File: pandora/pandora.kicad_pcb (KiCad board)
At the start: 2 copper layers, 121.9 x 106.7 mm, 176 parts, among them J1 SMA, J2 PinHeader_100mil_01x04, J3 JST-SH_2, J4 TX3 / MTA-156-3, J5 Conn_ARM_JTAG_SWD_10, J6 USB_B_Mini, Q1 DMP1045U, SW1 GF-126-0317, SW10 PTS645-S-H-50-SMTR92-LFS, SW11 PTS645-S-H-50-SMTR92-LFS, SW12 PTS645-S-H-50-SMTR92-LFS, SW13 PTS645-S-M-43-SMTR92-LFS, SW14 PTS645-S-K-50-SMTR92-LFS, SW15 PTS645-S-K-50-SMTR92-LFS, SW16 PTS645-S-K-50-SMTR92-LFS, SW17 PTS645-S-K-50-SMTR92-LFS, SW18 PTS526-S-K-15-SMTR92-LFS, SW2 PTS645-S-H-50-SMTR92-LFS, SW3 PTS645-S-H-50-SMTR92-LFS, SW4 PTS645-S-H-50-SMTR92-LFS, SW5 PTS645-S-H-50-SMTR92-LFS, SW6 PTS645-S-H-50-SMTR92-LFS, SW7 PTS645-S-H-50-SMTR92-LFS, SW8 PTS645-S-H-50-SMTR92-LFS, SW9 PTS645-S-M-43-SMTR92-LFS, U1 LM1086CS-ADJ, U10 ADM811ZARTZ, U11 LCD_Adafruit_16x02_Neg_RGB, U12 MCP73831-2-OT, U13 MCP1642D-50, U2 MCP1702T-3302, U3 MCP1702T-3302, U4 MCP6001, U5 MPU-9250, U6 ULN2003D, U7 74LCX245, U8 CC2652R, U9 74LVC1G08, Y1 NC26_32.768k, Y2 FA-238_48M

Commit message: Continue layout
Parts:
- moved R19 10.3 mm to (-49.9, 100.1), turned to 90 degrees
- moved RV1 3.41 mm to (-104.0, 83.3)
- moved NT3 2.41 mm to (-13.3, 107.3)
- moved C33 2.16 mm to (-30.6, 90.9), turned to 270 degrees
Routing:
- net /keypad/KPD_IN2: track 16.5 -> 56.2 mm
- net /connectors/LCD_OUT_CNTR: track 0.00 -> 36.9 mm
- net Net-(D2-Pad2): track 0.00 -> 35.5 mm
- net +5V: track 13.0 -> 47.4 mm
- net Net-(D4-Pad2): track 0.00 -> 28.2 mm
- net VMCU: track 48.9 -> 76.4 mm, vias 3 -> 7
- net VIN: track 4.79 -> 23.6 mm
- net /connectors/SERVO_PWM: track 32.0 -> 44.7 mm, vias 0 -> 2
- net /connectors/JTAG_~RESET: track 5.91 -> 17.3 mm
- net VSERVO: track 9.82 -> 19.1 mm
- net GNDBAT: track 18.5 -> 27.1 mm
- net GNDIN: track 16.6 -> 25.0 mm
- net /keypad/KPD_IN4: track 28.9 -> 35.8 mm
- net /keypad/KPD_IN3: track 16.5 -> 23.5 mm
- net /mcu/VMCUA: track 20.0 -> 22.4 mm
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- added copper zone on B.Cu, net GNDD

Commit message: Start routing
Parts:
- NT1: moved to B.Cu
- moved R6 33.5 mm to (-72.9, 92.2)
- moved R5 24.1 mm to (-83.1, 92.2)
- moved D2 16.6 mm to (-102.7, 88.6), turned to 180 degrees
- moved R4 16.0 mm to (-93.2, 92.2)
- moved SW15 15.3 mm to (-110.2, 125.1)
- moved SW17 15.2 mm to (-110.1, 140.3)
- moved D3 10.7 mm to (-93.1, 88.6), turned to 180 degrees
- moved R3 4.96 mm to (-117.5, 97.8), turned to 180 degrees
- moved D4 4.50 mm to (-82.9, 88.6), turned to 180 degrees
- moved RV1 2.25 mm to (-102.4, 81.8), turned to 180 degrees
- moved D5 2.18 mm to (-73.0, 88.6), turned to 180 degrees
- moved D10 1.02 mm to (-81.2, 81.8)
- moved D11 1.02 mm to (-77.8, 81.8)
- moved D12 1.02 mm to (-74.5, 81.8)
- moved D8 1.02 mm to (-90.6, 81.8)
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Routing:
- net /keypad/KPD_IN1: track 48.9 -> 159.8 mm
- net Net-(D5-Pad2): track 31.1 -> 92.8 mm, vias 0 -> 2
- net +3V3: track 13.5 -> 75.1 mm, vias 0 -> 6
- net Net-(D3-Pad2): track 0.77 -> 61.3 mm, vias 0 -> 2
- net /keypad/KPD_IN3: track 23.5 -> 77.0 mm
- net /keypad/KPD_IN4: track 35.8 -> 86.7 mm
- net /keypad/KPD_OUT1: track 16.5 -> 58.2 mm, vias 0 -> 6
- net Net-(D4-Pad2): track 28.2 -> 64.3 mm, vias 0 -> 2
- net /keypad/KPD_OUT2: track 16.5 -> 49.2 mm, vias 0 -> 4
- net /keypad/KPD_IN2: track 56.2 -> 81.7 mm
- net /keypad/KPD_OUT3: track 16.5 -> 38.4 mm, vias 0 -> 2
- net /keypad/KPD_OUT4: track 16.5 -> 27.4 mm
- net Net-(D2-Pad2): track 35.5 -> 46.1 mm
- net Net-(JP9-Pad1): track 0.00 -> 8.89 mm, vias 0 -> 1
- net Net-(JP8-Pad1): track 0.00 -> 8.89 mm, vias 0 -> 1
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
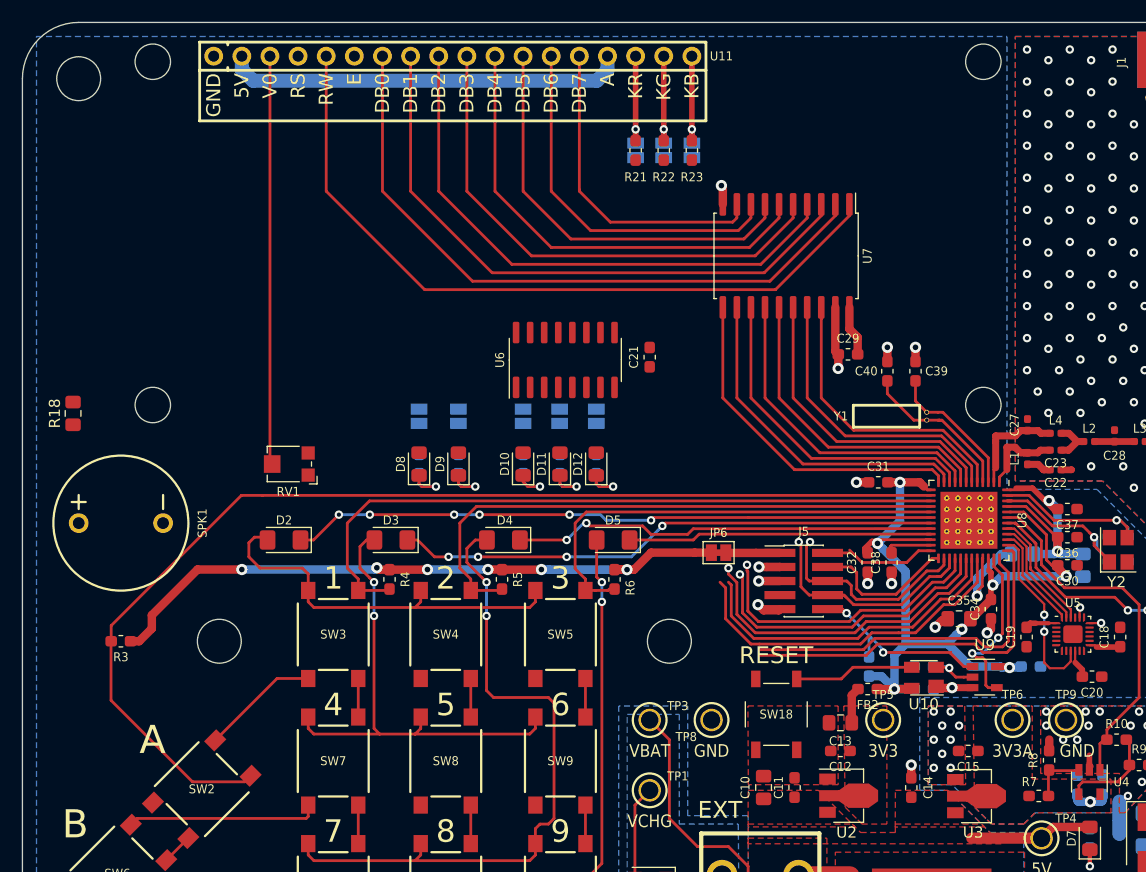
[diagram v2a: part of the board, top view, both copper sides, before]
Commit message: Almost finish routing
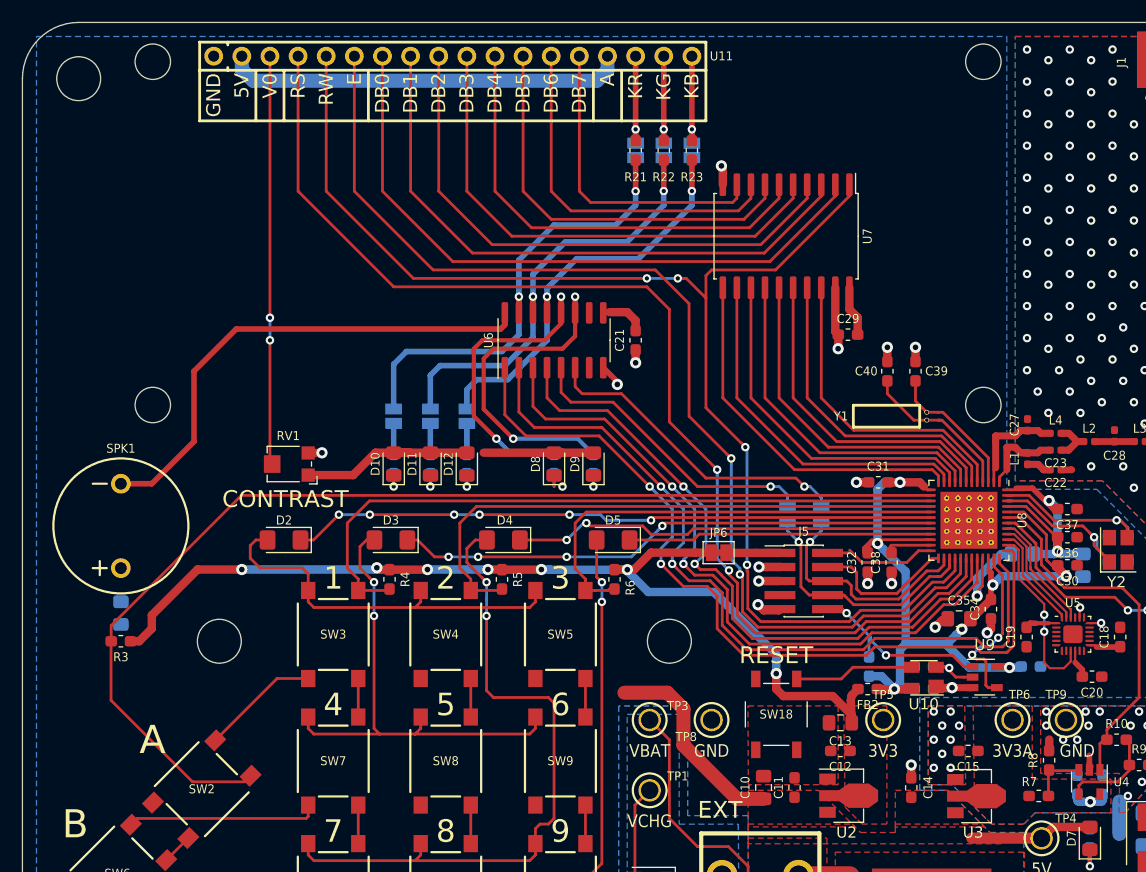
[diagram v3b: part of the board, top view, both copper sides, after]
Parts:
- R18: moved to B.Cu
- moved JP5 34.4 mm to (-57.3, 86.4)
- moved JP4 34.0 mm to (-54.2, 86.4)
- moved R18 18.5 mm to (-117.5, 95.2), turned to 270 degrees
- moved D8 12.2 mm to (-78.4, 81.8)
- moved D9 12.2 mm to (-74.8, 81.8)
- moved R13 12.2 mm to (-78.4, 81.8)
- moved R14 12.2 mm to (-74.8, 81.8)
- moved D10 11.7 mm to (-92.8, 81.8)
- moved D11 11.7 mm to (-89.5, 81.8)
- moved D12 11.7 mm to (-86.2, 81.8)
- moved JP1 11.7 mm to (-92.8, 77.5)
- moved JP2 11.7 mm to (-89.5, 77.5)
- moved JP3 11.7 mm to (-86.2, 77.5)
- moved R15 11.7 mm to (-92.8, 81.8)
- moved R16 11.7 mm to (-89.5, 81.8)
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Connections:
- JP4 pad 2: /led_speaker/LED1 -> /led_speaker/LED2
- JP5 pad 2: /led_speaker/LED2 -> /led_speaker/LED1
- U6 pad 1: /led_speaker/LCD_BL_R -> /led_speaker/SPEAKER
- U6 pad 13: /led_speaker/SPK_DRV -> /connectors/LCD_OUT_BL_B
- U6 pad 14: /connectors/LCD_OUT_BL_B -> /connectors/LCD_OUT_BL_G
- U6 pad 15: /connectors/LCD_OUT_BL_G -> /connectors/LCD_OUT_BL_R
- U6 pad 16: /connectors/LCD_OUT_BL_R -> /led_speaker/SPK_DRV
- U6 pad 2: /led_speaker/LCD_BL_G -> /led_speaker/LCD_BL_R
- U6 pad 3: /led_speaker/LCD_BL_B -> /led_speaker/LCD_BL_G
- U6 pad 4: /led_speaker/SPEAKER -> /led_speaker/LCD_BL_B
- U8 pad 28: /connectors/LCD_OUT_RS -> /connectors/LCD_OUT_RW
- U8 pad 29: /connectors/LCD_OUT_RW -> /lcd/LCD_E
- U8 pad 30: /lcd/LCD_E -> /connectors/LCD_OUT_RS
- U8 pad 31: /led_speaker/LCD_BL_R -> /led_speaker/LCD_BL_B
- U8 pad 36: /led_speaker/LCD_BL_B -> /led_speaker/LCD_BL_R
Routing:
- net /connectors/LCD_OUT_RS: track 26.6 -> 105.4 mm, vias 1 -> 2
- net /lcd/LCD_E: track 29.6 -> 100.1 mm, vias 1 -> 2
- net +5V: track 47.4 -> 97.4 mm
- net /led_speaker/SPK_DRV: track 0.00 -> 45.4 mm
- net /led_speaker/LCD_BL_R: track 29.8 -> 71.9 mm, vias 0 -> 2
- net /led_speaker/SPEAKER: track 33.1 -> 75.1 mm, vias 0 -> 2
- net /connectors/LCD_OUT_BL_R: track 0.00 -> 41.3 mm, vias 0 -> 2
- net /connectors/LCD_OUT_BL_G: track 0.00 -> 39.4 mm, vias 0 -> 2
- net /connectors/LCD_OUT_BL_B: track 0.00 -> 37.3 mm, vias 0 -> 2
- net /led_speaker/LCD_BL_G: track 31.7 -> 63.0 mm, vias 0 -> 2
- net /led_speaker/LED2: track 0.00 -> 29.5 mm, vias 0 -> 1
- net /led_speaker/LCD_BL_B: track 31.2 -> 60.2 mm, vias 0 -> 2
- net /led_speaker/LED2_DRV: track 0.00 -> 28.8 mm, vias 0 -> 2
- net +3V3: track 75.1 -> 103.4 mm, vias 6 -> 7
- net /led_speaker/LED1: track 0.00 -> 27.6 mm, vias 0 -> 1
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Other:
- board text added: "CONTRAST"

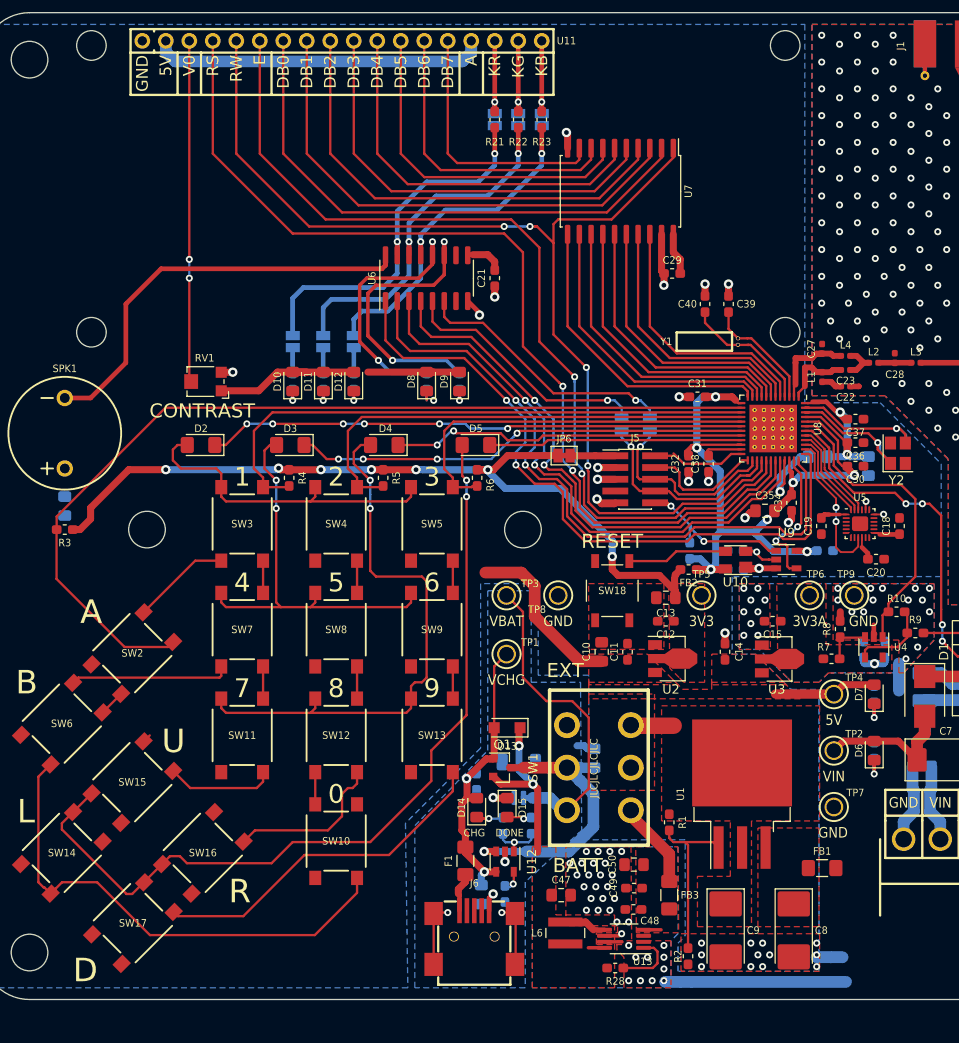
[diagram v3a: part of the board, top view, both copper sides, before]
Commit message: Almost finish routing
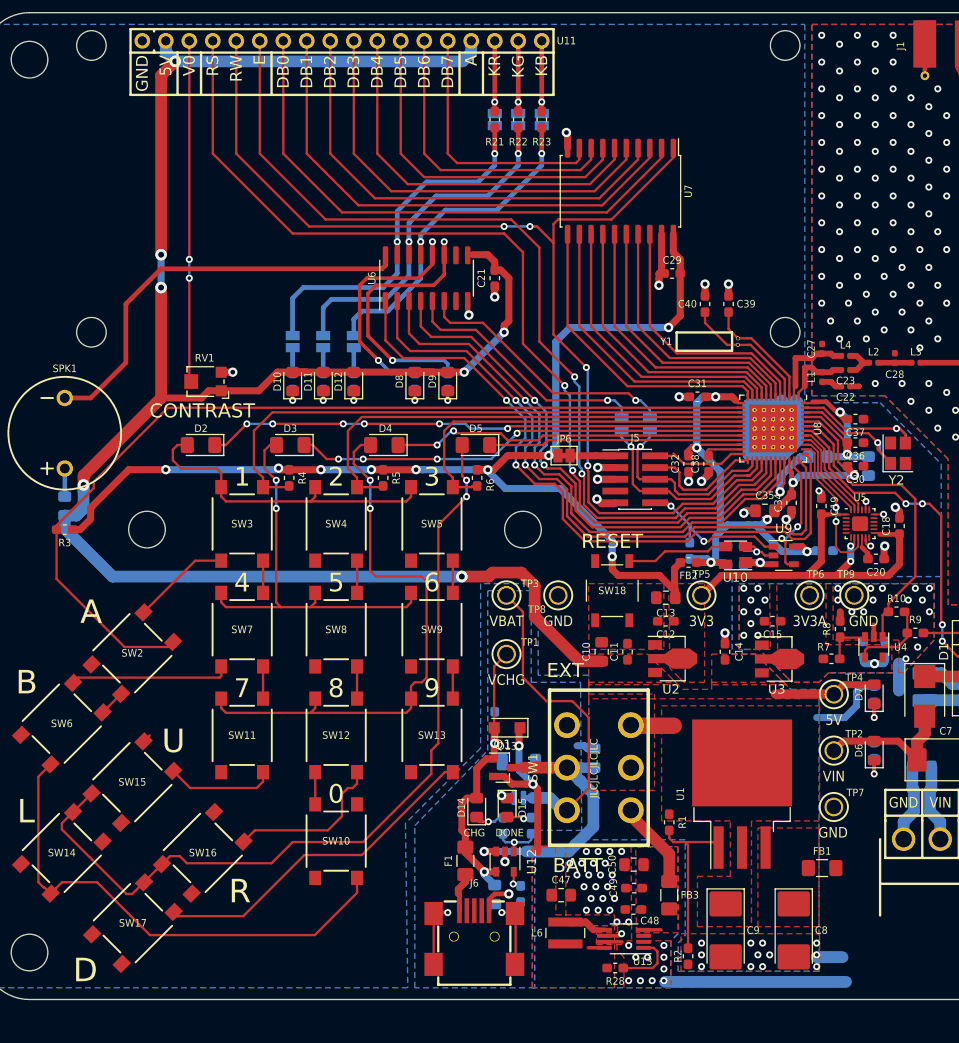
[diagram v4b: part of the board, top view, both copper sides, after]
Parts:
- moved REF** 65.9 mm to (-98.9, 119.9)
- moved R25 6.97 mm to (-71.0, 118.4), turned to 270 degrees
- moved C19 2.16 mm to (-35.7, 95.2), turned to 270 degrees
- moved R26 1.69 mm to (-68.2, 137.2)
- moved C45 1.46 mm to (-71.0, 137.2)
- moved D8 1.27 mm to (-79.6, 81.8)
- moved R13 1.27 mm to (-79.6, 81.8)
- moved D9 1.27 mm to (-76.1, 81.8)
- moved R14 1.27 mm to (-76.1, 81.8)
- moved FB2 0.76 mm to (-50.0, 101.3)
- moved U9 0.53 mm to (-39.8, 100.6)
- moved C43 0.51 mm to (-45.0, 101.6)
- moved R20 0.51 mm to (-45.0, 99.6)
- moved U10 0.51 mm to (-45.0, 100.6)
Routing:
- net +5V: track 97.4 -> 226.3 mm, vias 0 -> 7
- net +3V3: track 103.4 -> 174.2 mm, vias 7 -> 11
- net GNDD: track 34.8 -> 70.6 mm, vias 31 -> 35
- net Net-(R18-Pad1): track 0.00 -> 3.05 mm
- net /mcu/~RESET: track 15.4 -> 13.6 mm
- net /keypad/KPD_IN4: track 86.7 -> 85.5 mm
- net /led_speaker/LED2_DRV: track 28.8 -> 28.0 mm
- net GNDBAT: track 27.1 -> 27.9 mm

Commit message: Finish routing
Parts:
- moved NT3 0.13 mm to (-13.3, 107.4)
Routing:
- net GNDIN: track 25.0 -> 145.8 mm, vias 0 -> 1
- net VIN: track 23.6 -> 46.9 mm
- net GNDBAT: track 27.9 -> 13.2 mm, vias 39 -> 46
- net (no net): track 3.30 -> 0.00 mm
- net GNDSERVO: track 9.32 -> 11.3 mm
- net GNDD: track 70.6 -> 72.4 mm, vias 35 -> 234
- net VMCU: track 77.2 -> 78.8 mm
- net GNDRF: track 3.74 -> 4.63 mm
- net +5V: track 226.3 -> 227.1 mm
- net Net-(D7-Pad1): track 3.15 -> 2.64 mm
- net Net-(D6-Pad1): track 3.15 -> 2.64 mm

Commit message: Fix top silk
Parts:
- moved C27 208.3 mm to (172.7, 78.2)
- moved C35 208.3 mm to (166.5, 95.8)
- moved D8 208.3 mm to (128.7, 81.8)
- moved FB1 208.3 mm to (172.7, 134.4)
- moved L1 208.3 mm to (172.7, 81.3)
- moved Q1 208.3 mm to (138.1, 123.5)
- moved R13 208.3 mm to (128.7, 81.8)
- moved R2 208.3 mm to (158.2, 143.9)
- moved TP8 208.3 mm to (144.1, 104.9)
- moved AE1 208.3 mm to (199.1, 79.8)
- moved C1 208.3 mm to (183.5, 128.3)
- moved C10 208.3 mm to (148.8, 111.0)
- moved C11 208.3 mm to (151.6, 111.0)
- moved C12 208.3 mm to (155.8, 107.7)
- moved C13 208.3 mm to (155.8, 105.2)
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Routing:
- net GNDD: vias 234 -> 235

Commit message: Fix bottom silk
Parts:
- moved REF** 207.8 mm to (108.8, 120.8)

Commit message: Decorate
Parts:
- added G***: LOGO, pandora:logo-rs-large, B.Cu at (119.8, 93.7)
- added G***: LOGO, pandora:logo-rs, F.Cu at (148.0, 83.3)
- added G***: LOGO, pandora:logo-blacker, B.Cu at (163.2, 135.1)
- added G***: LOGO, pandora:logo-blacker, F.Cu at (116.5, 62.0)
- added G***: LOGO, pandora:logo-ruddock, F.Cu at (100.2, 62.2)
- added G***: LOGO, pandora:logo-ruddock, B.Cu at (162.9, 117.1)
- added G***: LOGO, pandora:logo-pandora-large, B.Cu at (124.3, 65.3)
- added G***: LOGO, pandora:logo-caltech-ee, B.Cu at (111.1, 143.5)
- added G***: LOGO, pandora:logo-pandora, F.Cu at (114.7, 144.5)
- moved R25 1.40 mm to (137.3, 117.0)
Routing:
- net +5V: track 227.1 -> 228.8 mm
- net VCHG: track 32.4 -> 33.9 mm
- net Net-(R1-Pad2): track 18.2 -> 19.1 mm
- net GNDD: vias 235 -> 237
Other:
- board text added: "CC2652R Dev Board"
- board text added: "Ray Sun"
